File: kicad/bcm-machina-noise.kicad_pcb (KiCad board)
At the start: 2 copper layers, 125.2 x 78 mm, 61 parts, among them J1 USB_A, J2 AVR-ISP-6, J3 AudioJack2_SwitchT, J5 AudioJack2_SwitchT, Q1 2N5457, Q2 2N5457, SW1 SW_Push, SW2 SW_Push, U1 4069, U2 MCP602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

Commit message: updated pcb layout
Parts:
- removed J1: USB_A, USBPower:AMPHENOL_10103593-0001LF
- removed RV3: 10k, Trimpot:Potentiometer_THT_Bourns_3306P_Vertical
- added C8: 100nF, Capacitor_THT:C_Rect_L7.0mm_W3.5mm_P5.00mm, F.Cu at (101.1, 76.5)
- added C9: 100pF, Capacitor_THT:C_Rect_L7.0mm_W3.5mm_P5.00mm, F.Cu at (143.0, 90.9)
- added J4: USB_B_Micro, USBPower:AMPHENOL_10103593-0001LF, F.Cu at (90.9, 73.5)
- added R23: 100k, Resistor_THT:R_Axial_DIN0207_L6.3mm_D2.5mm_P10.16mm_Horizontal, F.Cu at (105.4, 97.3)
- added R24: 100k, Resistor_THT:R_Axial_DIN0207_L6.3mm_D2.5mm_P10.16mm_Horizontal, F.Cu at (133.9, 76.5)
- added R27: 2k2, Resistor_THT:R_Axial_DIN0207_L6.3mm_D2.5mm_P10.16mm_Horizontal, F.Cu at (179.6, 93.2)
- added R28: 100k, Resistor_THT:R_Axial_DIN0207_L6.3mm_D2.5mm_P10.16mm_Horizontal, F.Cu at (130.3, 86.6)
- added R29: 100k, Resistor_THT:R_Axial_DIN0207_L6.3mm_D2.5mm_P10.16mm_Horizontal, F.Cu at (175.8, 93.2)
- added R30: 100k, Resistor_THT:R_Axial_DIN0207_L6.3mm_D2.5mm_P10.16mm_Horizontal, F.Cu at (148.8, 95.0)
- added TP1: OSC Test Point, TestPoint:TestPoint_Loop_D2.50mm_Drill1.0mm_LowProfile, F.Cu at (137.2, 95.2)
- added TP2: LFO Test Point, TestPoint:TestPoint_Loop_D2.50mm_Drill1.0mm_LowProfile, F.Cu at (102.4, 97.3)
- C1, C2: value 100nF -> 220nF
- C4, C5: value C_Polarized -> 10uF
- Q1, Q2: value 2N5457 -> J113
- R13, R14, R17: value 10k -> 100k
- R16, R25: value 10k -> 1k
- R20, R21: value 1k -> 2k2
- R26: value 10k -> 4k7
- RV1: value 10kA -> 100k
- moved R25 67.1 mm to (159.3, 99.1), turned to 0 degrees
- moved R26 55.1 mm to (141.0, 76.5), turned to -90 degrees
- moved R15 13.2 mm to (148.8, 108.2), turned to 90 degrees
- moved R14 12.5 mm to (144.5, 76.5)
- moved R18 11.7 mm to (104.6, 81.3)
- moved R19 11.7 mm to (104.6, 76.2)
- moved J2 11.7 mm to (123.4, 81.8)
- moved C4 8.19 mm to (131.6, 91.4)
- moved C3 5.84 mm to (126.2, 87.4)
- moved U3 5.33 mm to (120.9, 86.1)
- moved C1 4.32 mm to (154.7, 95.0), turned to 0 degrees
- moved R13 4.19 mm to (137.4, 86.6)
- moved R16 4.13 mm to (183.4, 93.2)
- moved R17 3.10 mm to (187.2, 103.4)
- moved C2 2.80 mm to (164.1, 95.0), turned to 0 degrees
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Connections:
- C1 pad 2: Net-(Q2-S) -> Net-(C1-Pad2)
- C4 pad 1: /MCU_MISO -> Net-(C4-Pad1)
- J2 pad 4: /MCU_DOUT1 -> /MCU_MOSI
- R13 pad 1: Net-(C4-Pad2) -> Net-(R13-Pad1)
- R14 pad 1: Net-(R14-Pad1) -> Net-(R13-Pad2)
- R14 pad 2: Net-(Q1-S) -> Net-(R14-Pad2)
- R16 pad 1: GND -> Net-(R14-Pad2)
- R16 pad 2: Net-(C2-Pad2) -> Net-(Q1-S)
- R17 pad 1: Net-(R17-Pad1) -> Net-(C2-Pad2)
- R17 pad 2: Net-(R14-Pad1) -> Net-(R13-Pad2)
- R18 pad 1: Net-(R18-Pad1) -> Net-(U2A-+)
- R18 pad 2: /MCU_PWM_2 -> /MCU_MOSI
- R25 pad 1: Net-(R25-Pad1) -> Net-(C1-Pad2)
- R25 pad 2: Net-(U2A--) -> Net-(Q2-S)
- R26 pad 1: Net-(U2A--) -> Net-(R26-Pad1)
- R26 pad 2: Net-(R18-Pad1) -> Net-(R13-Pad1)
- RV1 pad 1: unconnected-(RV1-Pad1) -> Net-(Q1-S)
- RV1 pad 4: unconnected-(RV1-Pad4) -> Net-(Q2-S)
- RV2 pad 1: unconnected-(RV2-Pad1) -> Net-(R26-Pad1)
- RV2 pad 2: Net-(R17-Pad1) -> Net-(R26-Pad1)
- RV2 pad 3: Net-(C2-Pad2) -> Net-(R27-Pad2)
- RV4 pad 3: Net-(R25-Pad1) -> Net-(R23-Pad2)
- U1 pad 1: Net-(R14-Pad1) -> Net-(R13-Pad2)
- U1 pad 12: Net-(R14-Pad1) -> Net-(R13-Pad1)
- U1 pad 13: Net-(R13-Pad2) -> Net-(R26-Pad1)
- U1 pad 2: Net-(Q1-S) -> Net-(R14-Pad2)
- U1 pad 4: Net-(Q2-S) -> Net-(C1-Pad2)
- U2 pad 1: Net-(R25-Pad1) -> Net-(U2A--)
- U2 pad 3: GND -> Net-(U2A-+)
- U3 pad 6: /MCU_PWM_2 -> /MCU_DOUT1
- U3 pad 7: /MCU_DOUT1 -> /MCU_MOSI
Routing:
- net Net-(R26-Pad1): track 0.00 -> 79.4 mm
- net Net-(R25-Pad1): track 63.2 -> 0.00 mm
- net Net-(R14-Pad1): track 57.2 -> 0.00 mm
- net Net-(R13-Pad2): track 15.9 -> 66.9 mm
- net Net-(R14-Pad2): track 0.00 -> 48.3 mm
- net Net-(C1-Pad2): track 0.00 -> 42.1 mm
- net Net-(R13-Pad1): track 0.00 -> 26.0 mm
- net /MCU_DOUT1: track 47.3 -> 21.4 mm
- net Net-(R23-Pad2): track 0.00 -> 22.7 mm
- net Net-(R18-Pad1): track 20.0 -> 0.00 mm
- net /MCU_MOSI: track 0.00 -> 18.1 mm
- net Net-(C4-Pad1): track 0.00 -> 17.7 mm
- net Net-(U2A-+): track 0.00 -> 16.2 mm
- net Net-(C4-Pad2): track 20.5 -> 4.93 mm
- net /MCU_PWM_2: track 15.0 -> 0.00 mm
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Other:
- outline, holes or cut-outs redrawn

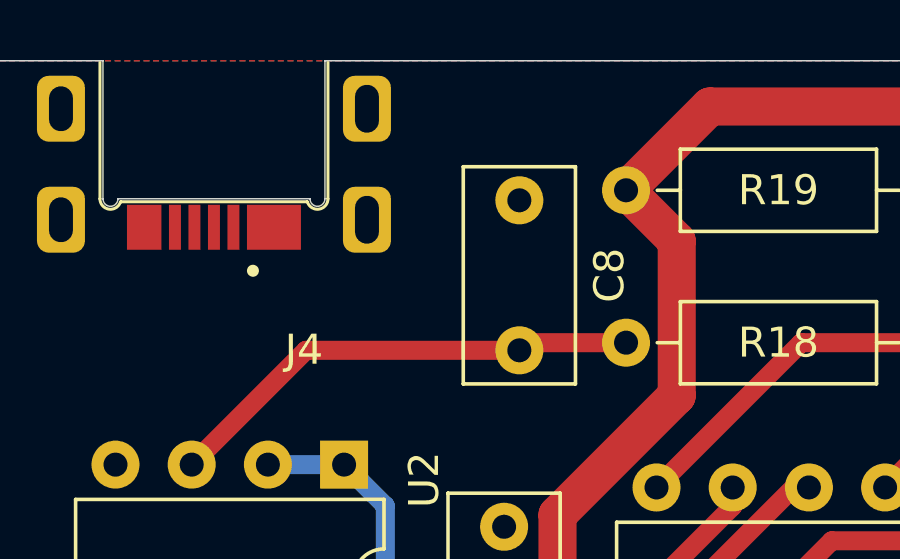
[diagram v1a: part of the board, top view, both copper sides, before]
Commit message: clearance error fix
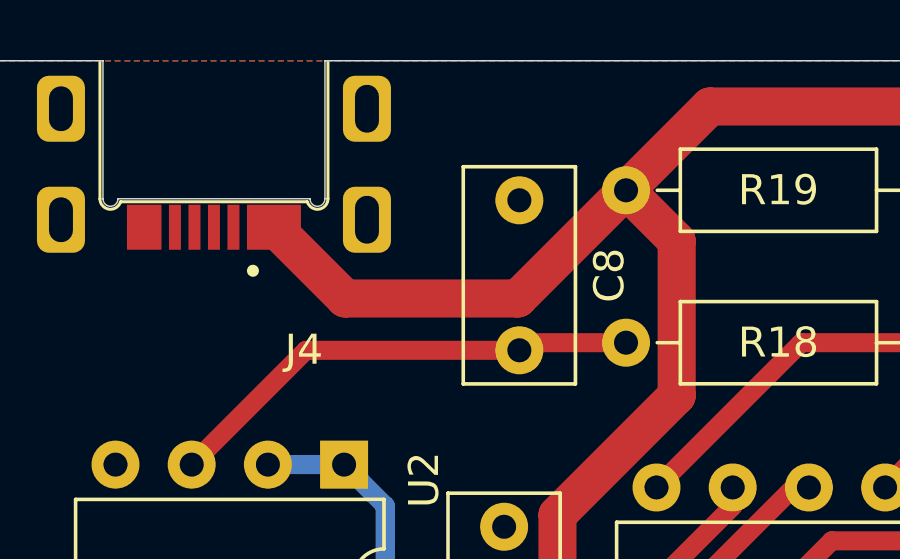
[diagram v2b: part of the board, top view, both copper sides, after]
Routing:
- net VCC: track 211.6 -> 225.8 mm
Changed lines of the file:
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@@
   (segment (start 104.648 76.2) (end 107.442 73.406) (width 1.27) (layer "F.Cu") (net 5))
   (segment (start 161.798 73.406) (end 164.31 73.406) (width 1.27) (layer "F.Cu") (net 5))
+  (segment (start 101.0412 79.8068) (end 95.2866 79.8068) (width 1.27) (layer "F.Cu") (net 5))
+  (segment (start 104.648 76.2) (end 101.0412 79.8068) (width 1.27) (layer "F.Cu") (net 5))
   (segment (start 93.472 94.742) (end 73.152 94.742) (width 1.27) (layer "F.Cu") (net 5))
   (segment (start 151.17 73.406) (end 151.638 73.406) (width 1.27) (layer "F.Cu") (net 5))
@@
   (segment (start 151.638 73.406) (end 161.798 73.406) (width 1.27) (layer "F.Cu") (net 5))
   (segment (start 118.872 73.406) (end 107.442 73.406) (width 1.27) (layer "F.Cu") (net 5))
+  (segment (start 95.2866 79.8068) (end 92.912 77.4322) (width 1.27) (layer "F.Cu") (net 5))
   (segment (start 148.844 75.732) (end 151.17 73.406) (width 1.27) (layer "F.Cu") (net 5))
   (segment (start 73.66 134.62) (end 73.66 142.24) (width 1.27) (layer "F.Cu") (net 5))
